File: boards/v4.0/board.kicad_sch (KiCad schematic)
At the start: 61 parts, among them J1 KF301-2P, J2 KF301-2P, J3 KF301-2P, J4 KF301-2P, J5 KF301-2P, J6 KF301-2P, J7 KF301-2P, P1 Pin Header, P2 Pin Header, P3 Pin Header, P4 Pin Header, P5 Pin Header, SW1 SS-12D00G 4mm

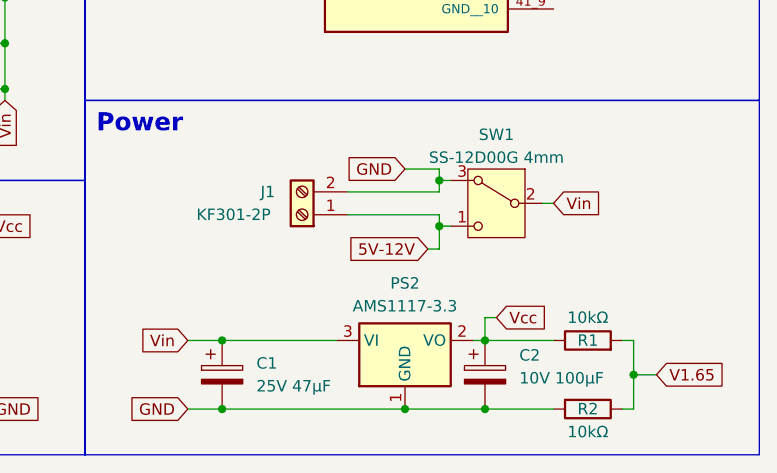
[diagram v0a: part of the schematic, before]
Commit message: Board IDs Correction and update documentation
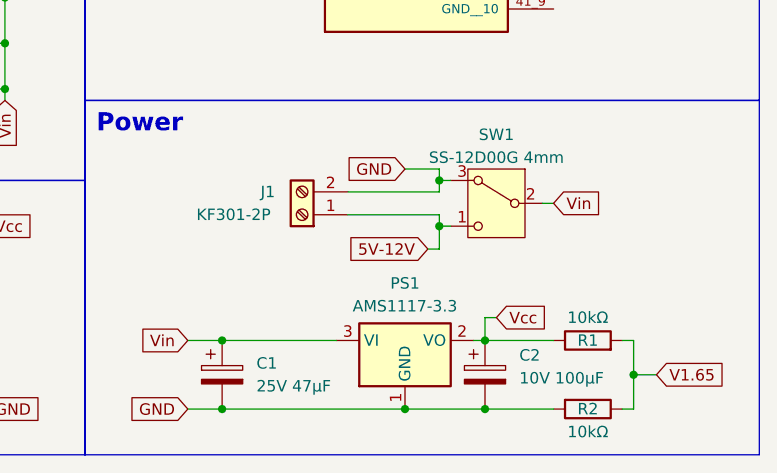
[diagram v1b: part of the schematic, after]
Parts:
- renumbered PS2 to PS1
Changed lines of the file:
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@@
   (symbol (lib_id "Regulator_Linear:AMS1117-3.3") (at 243.84 151.13 0) (unit 1)
     (in_bom yes) (on_board yes) (dnp no) (fields_autoplaced)
-    (property "Reference" "PS2" (at 243.84 144.78 0)
+    (property "Reference" "PS1" (at 243.84 144.78 0)
       (effects (font (size 1.27 1.27)))
     )
@@
       (project "board"
         (path "/7fdecbff-7204-4ee7-8cff-285fbd7a00a8"
-          (reference "PS2") (unit 1)
+          (reference "PS1") (unit 1)
         )
       )

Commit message: Initial tests of microcontroller code
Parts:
- added R20: 50Ω, Resistor_SMD:R_1210_3225Metric, symbol Device:R
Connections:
- net TC A-1: now also R20.1; no longer AMP8.1, AMP8.2 (-)
- new net: AMP8.1, AMP8.2 (-), R20.2
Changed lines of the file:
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@@
   (junction (at 223.52 151.13) (diameter 0) (color 0 0 0 0)
   )
+  (junction (at 109.22 25.4) (diameter 0) (color 0 0 0 0)
+  )
   (junction (at 199.39 118.11) (diameter 0) (color 0 0 0 0)
   )
@@
   (junction (at 140.97 148.59) (diameter 0) (color 0 0 0 0)
   )
-  (junction (at 109.22 25.4) (diameter 0) (color 0 0 0 0)
-  )
   (junction (at 138.43 80.01) (diameter 0) (color 0 0 0 0)
   )
@@
   (junction (at 121.92 96.52) (diameter 0) (color 0 0 0 0)
   )
+  (junction (at 130.81 25.4) (diameter 0) (color 0 0 0 0)
+  )
   (junction (at 199.39 107.95) (diameter 0) (color 0 0 0 0)
   )
@@
   (junction (at 199.39 113.03) (diameter 0) (color 0 0 0 0)
   )
-  (junction (at 130.81 25.4) (diameter 0) (color 0 0 0 0)
-  )
   (junction (at 252.73 151.13) (diameter 0) (color 0 0 0 0)
   )
@@
     (stroke (width 0) (type default))
   )
-  (wire (pts (xy 109.22 33.02) (xy 109.22 25.4))
+  (wire (pts (xy 109.22 21.59) (xy 109.22 25.4))
     (stroke (width 0) (type default))
   )
@@
     (stroke (width 0) (type default))
   )
-  (wire (pts (xy 109.22 21.59) (xy 109.22 25.4))
-    (stroke (width 0) (type default))
-  )
   (wire (pts (xy 121.92 46.99) (xy 109.22 46.99))
     (stroke (width 0) (type default))
@@
     (stroke (width 0) (type default))
   )
+  (wire (pts (xy 109.22 25.4) (xy 109.22 33.02))
+    (stroke (width 0) (type default))
+  )
   (wire (pts (xy 139.7 113.03) (xy 139.7 116.84))
     (stroke (width 0) (type default))
@@
     (stroke (width 0) (type default))
   )
+  (wire (pts (xy 127 25.4) (xy 130.81 25.4))
+    (stroke (width 0) (type default))
+  )
   (wire (pts (xy 267.97 151.13) (xy 269.24 151.13))
     (stroke (width 0) (type default))
@@
     (stroke (width 0) (type default))
   )
+  (wire (pts (xy 109.22 25.4) (xy 119.38 25.4))
+    (stroke (width 0) (type default))
+  )
   (wire (pts (xy 269.24 154.94) (xy 271.78 154.94))
     (stroke (width 0) (type default))
@@
     (stroke (width 0) (type default))
   )
-  (wire (pts (xy 109.22 25.4) (xy 130.81 25.4))
-    (stroke (width 0) (type default))
-  )
   (wire (pts (xy 243.84 132.08) (xy 247.65 132.08))
     (stroke (width 0) (type default))
@@
         )
       )
+    )
+  )
+  (symbol (lib_id "Device:R") (at 123.19 25.4 90) (unit 1)
+    (in_bom yes) (on_board yes) (dnp no)
+    (property "Reference" "R20" (at 123.19 25.4 90)
+      (effects (font (size 1.27 1.27)))
+    )
+    (property "Value" "50Ω" (at 123.19 22.86 90)
+      (effects (font (size 1.27 1.27)))
+    )
+    (property "Footprint" "Resistor_SMD:R_1210_3225Metric" (at 123.19 27.178 90)
+      (effects (font (size 1.27 1.27)) hide)
+    )
+    (property "Datasheet" "~" (at 123.19 25.4 0)
+      (effects (font (size 1.27 1.27)) hide)
+    )
+    (pin "1")
+    (pin "2")
+    (instances
+      (project "board"
+        (path "/7fdecbff-7204-4ee7-8cff-285fbd7a00a8"
+          (reference "R20") (unit 1)
+        )
+      )

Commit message: Code update
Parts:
- R6, R7, R8: value RSvolt -> 430Ω
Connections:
- net TC A-1: now also AMP4.2 (-), R9.2; no longer AMP1.3 (+), AMP2.3 (+), AMP3.3 (+), AMP4.3 (+), AMP5.3 (+), AMP6.3 (+), AMP7.3 (+), J5.1 (Pin_1), J6.1 (Pin_1), J7.1 (Pin_1), P2.1 (Pin_1), R20.1, TP1.4, TP2.4, TP3.4
- net TC A-2: now also AMP1.3 (+), AMP2.3 (+), AMP3.3 (+), AMP4.3 (+), AMP5.3 (+), AMP6.3 (+), AMP7.3 (+), J5.2 (Pin_2), J6.2 (Pin_2), J7.2 (Pin_2), P2.1 (Pin_1), R20.1, TP1.3, TP2.3, TP3.3; no longer AMP4.2 (-), R9.2
- net TC B-2 renamed TC B-1
- net TC B-1: now also J5.1 (Pin_1); no longer J5.2 (Pin_2)
- net TC C-2 renamed TC C-1
- net TC C-1: now also J6.1 (Pin_1); no longer J6.2 (Pin_2)
- net TC N-2 renamed TC N-1
- net TC N-1: now also J7.1 (Pin_1); no longer J7.2 (Pin_2)
- net TP A-1 renamed TP A-2
- net TP A-2: now also TP1.4; no longer TP1.3
- net TP B-1 renamed TP B-2
- net TP B-2: now also TP2.4; no longer TP2.3
- net TP C-1 renamed TP C-2
- net TP C-2: now also TP3.4; no longer TP3.3
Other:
- note added: "100A"
- note added: "12Ω"
- note added: "180kΩ"
- note added: "2.7Ω"
- note added: "2000:1"
- note added: "20A"
- note added: "2Ω"
- note added: "3000:1"
- note added: "300kΩ"
- note added: "4.3Ω"
- note added: "470kΩ"
- note added: "510kΩ"
- note added: "68Ω"
- note added: "7"
- note added: "8"
- note added: "Ratio"
- note added: "Resistor to Current"
- note added: "Resistor to Voltage"
- note added: "System"
- note removed: "100kΩ"
- note removed: "150kΩ"
- note removed: "2.2Ω"
- note removed: "270kΩ"
- note removed: "3.9Ω"
- note removed: "390Ω"
- note removed: "3Ω"
- note removed: "430Ω"
- note removed: "470Ω"
- note removed: "Current Type"
- note removed: "RSvolt"
- note removed: "Resistor to Current (Tranform Ratio 3000:1)"
- note removed: "Resistor to Voltage (Primary)"
- note removed: "Resistor to Voltage (Secundary)"
- note removed: "System Type"
- note removed: "Voltage Type"
